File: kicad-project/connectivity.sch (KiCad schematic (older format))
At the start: 3 parts

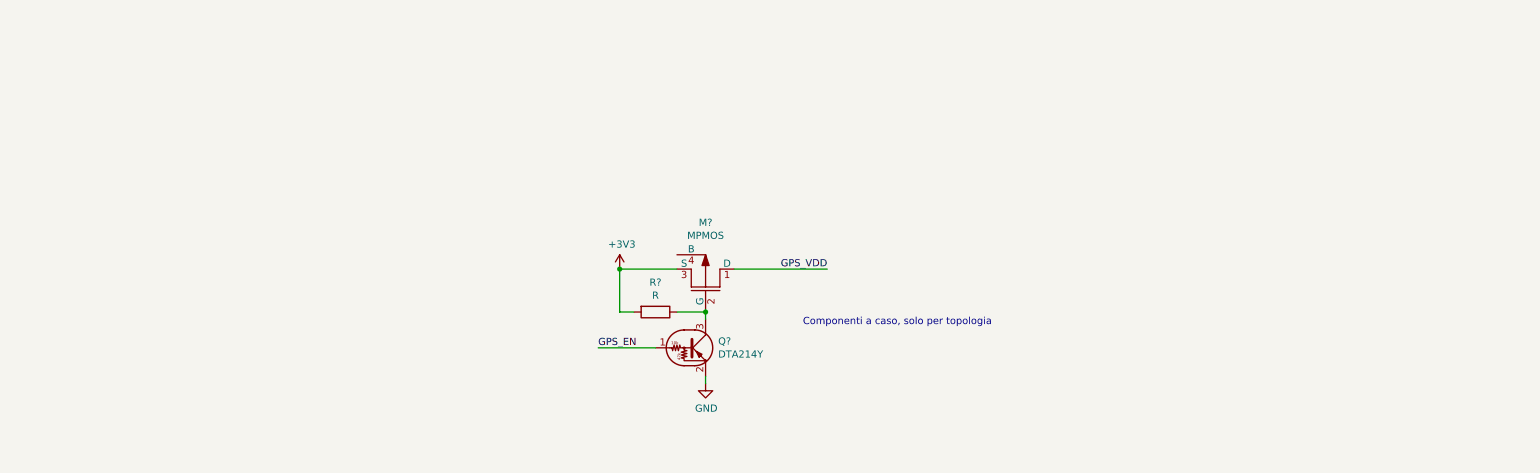
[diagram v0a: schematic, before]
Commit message: sch: add gps
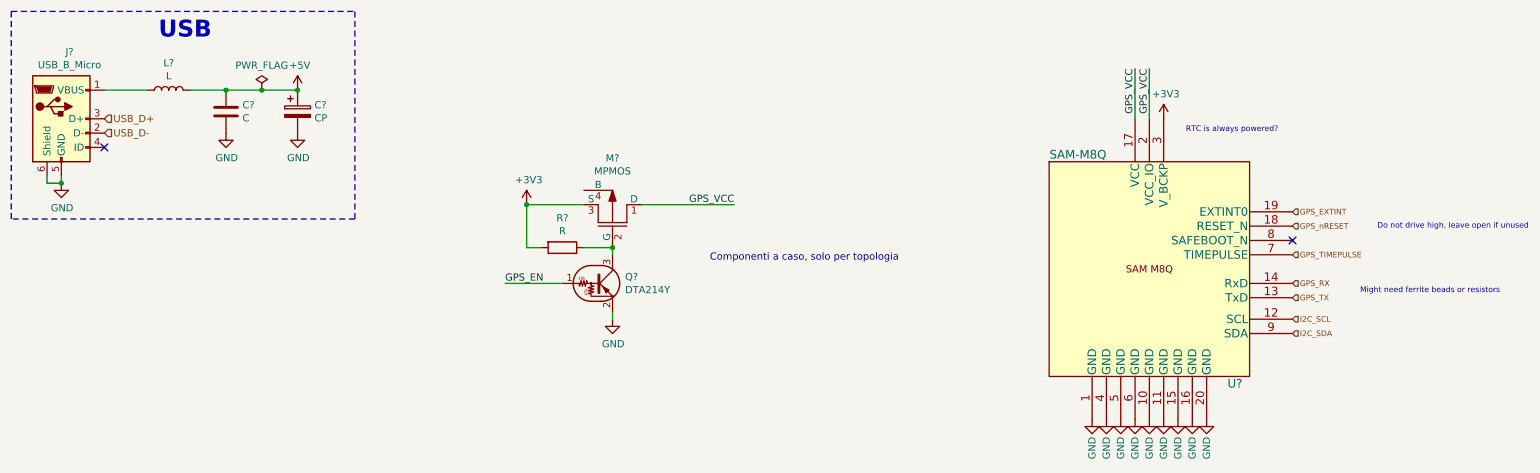
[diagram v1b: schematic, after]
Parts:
- added C?: C, symbol Device:C
- added C?: CP, symbol Device:CP
- added J?: USB_B_Micro, symbol Connector:USB_B_Micro
- added L?: L, symbol Device:L
- added U?: SAM-M8Q, AA_PPSE_2021:SAM-M8Q, symbol AA_PPSE_2021:SAM-M8Q
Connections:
- net +3V3: now also U?.3 (V_BCKP)
- net GND: now also C?.2, C?.2, J?.5 (GND), J?.6 (Shield), U?.1 (GND), U?.10 (GND), U?.11 (GND), U?.15 (GND), U?.16 (GND), U?.20 (GND), U?.4 (GND), U?.5 (GND), U?.6 (GND)
- net GPS_VDD renamed GPS_VCC
- net GPS_VCC: now also U?.17 (VCC), U?.2 (VCC_IO)
- new net: J?.1 (VBUS), L?.1
- new net +5V: C?.1, C?.1, L?.2
- new net GPS_EXTINT: U?.19 (EXTINT0)
- new net GPS_RX: U?.14 (RxD)
- new net GPS_TIMEPULSE: U?.7 (TIMEPULSE)
- new net GPS_TX: U?.13 (TxD)
- new net GPS_nRESET: U?.18 (RESET_N)
- new net I2C_SCL: U?.12 (SCL)
- new net I2C_SDA: U?.9 (SDA)
- new net USB_D+: J?.3 (D+)
- new net USB_D-: J?.2 (D-)
- no-connect marks 0 -> 2
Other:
- note added: "Do not drive high, leave open if unused"
- note added: "Might need ferrite beads or resistors"
- note added: "RTC is always powered?"
- note added: "USB"
- moved on the sheet: M?, Q?, R?
